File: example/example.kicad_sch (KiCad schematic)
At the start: 12 parts, among them J1 Conn_01x07_Male, U1 LDC1314

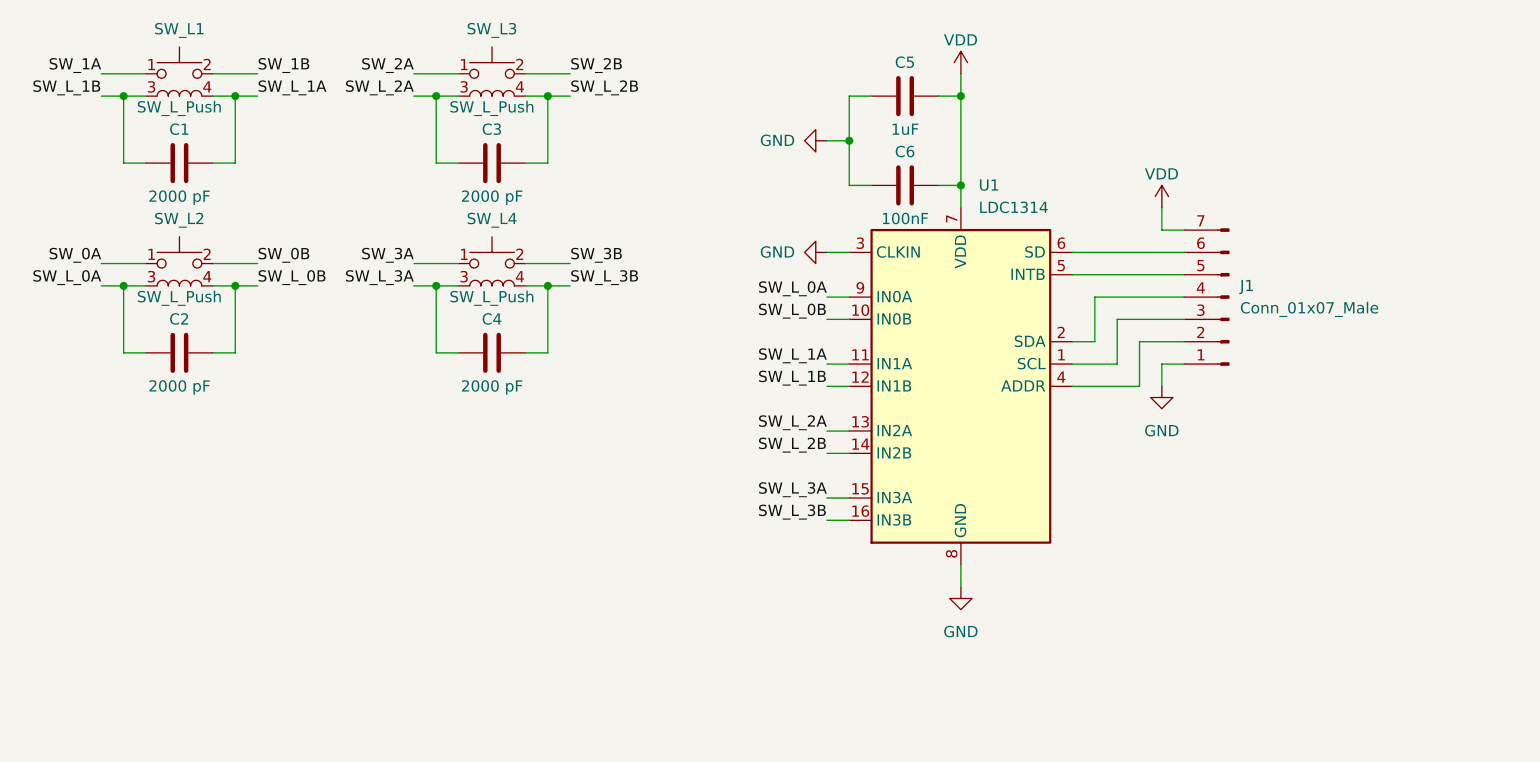
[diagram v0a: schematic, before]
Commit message: kikit for automatic fab output of example
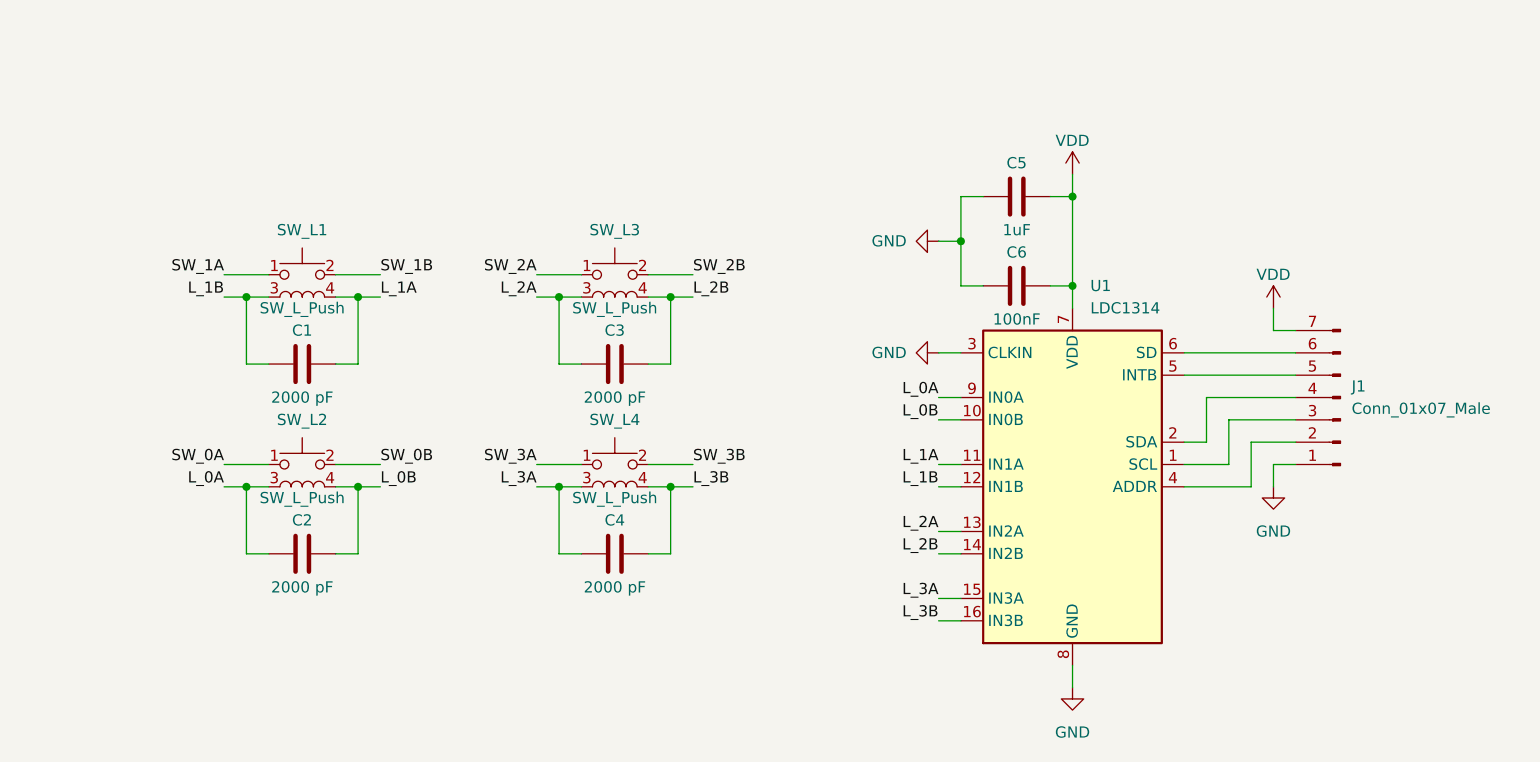
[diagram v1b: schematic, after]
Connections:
- net SW_L_0A renamed L_0A
- net SW_L_0B renamed L_0B
- net SW_L_1A renamed L_1A
- net SW_L_1B renamed L_1B
- net SW_L_2A renamed L_2A
- net SW_L_2B renamed L_2B
- net SW_L_3A renamed L_3A
- net SW_L_3B renamed L_3B
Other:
- company: (none) -> Elias Sjögreen
- title: (none) -> Inductive Analog Switch Breakout
- moved on the sheet: C1, C2, C3, C4, C5, C6, J1, SW_L1, SW_L2, SW_L3, SW_L4, U1
